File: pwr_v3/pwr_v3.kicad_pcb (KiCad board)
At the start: 4 copper layers, 166 x 166 mm, 83 parts, among them CN11 Conn_02x36_Odd_Even, CN12 Conn_02x36_Odd_Even, J1 Conn_01x12, J5 530470610, M1 Conn_02x03_Counter_Clockwise, M2 Conn_02x03_Counter_Clockwise, M3 Conn_02x03_Counter_Clockwise, M4 Conn_02x03_Counter_Clockwise, Q1 BUK9832-55A, Q2 BSS84, SW1 SW_SPST, U1 LM2576S-5, U2 LM2576S-12, U3 LM2576S-3.3, U4 LSM6DSLTR

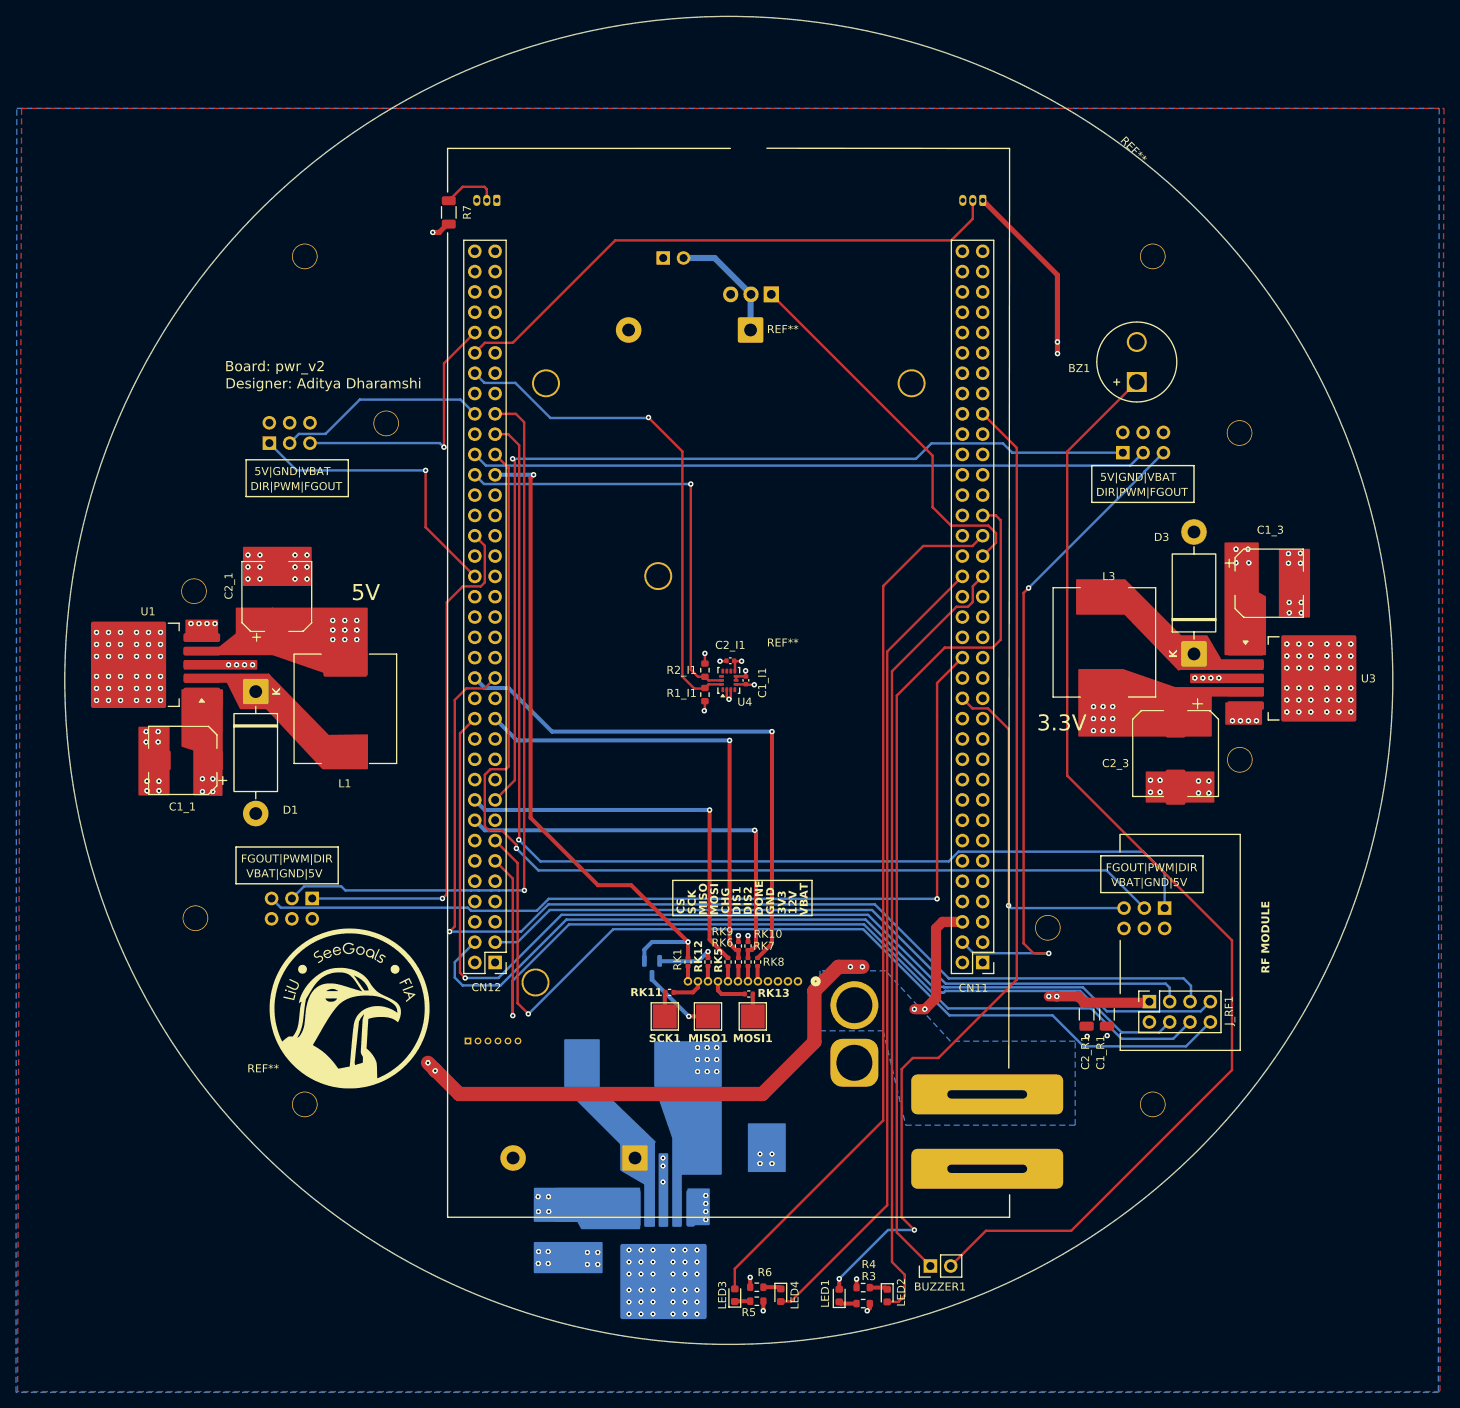
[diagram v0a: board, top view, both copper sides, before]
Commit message: Schematic and layout updated
Sch - Unwanted global labels removed from IMU, added new kicker labels, changed kicker connector footprint.
Layout - Updated kicker and encoder positions, routing updated.
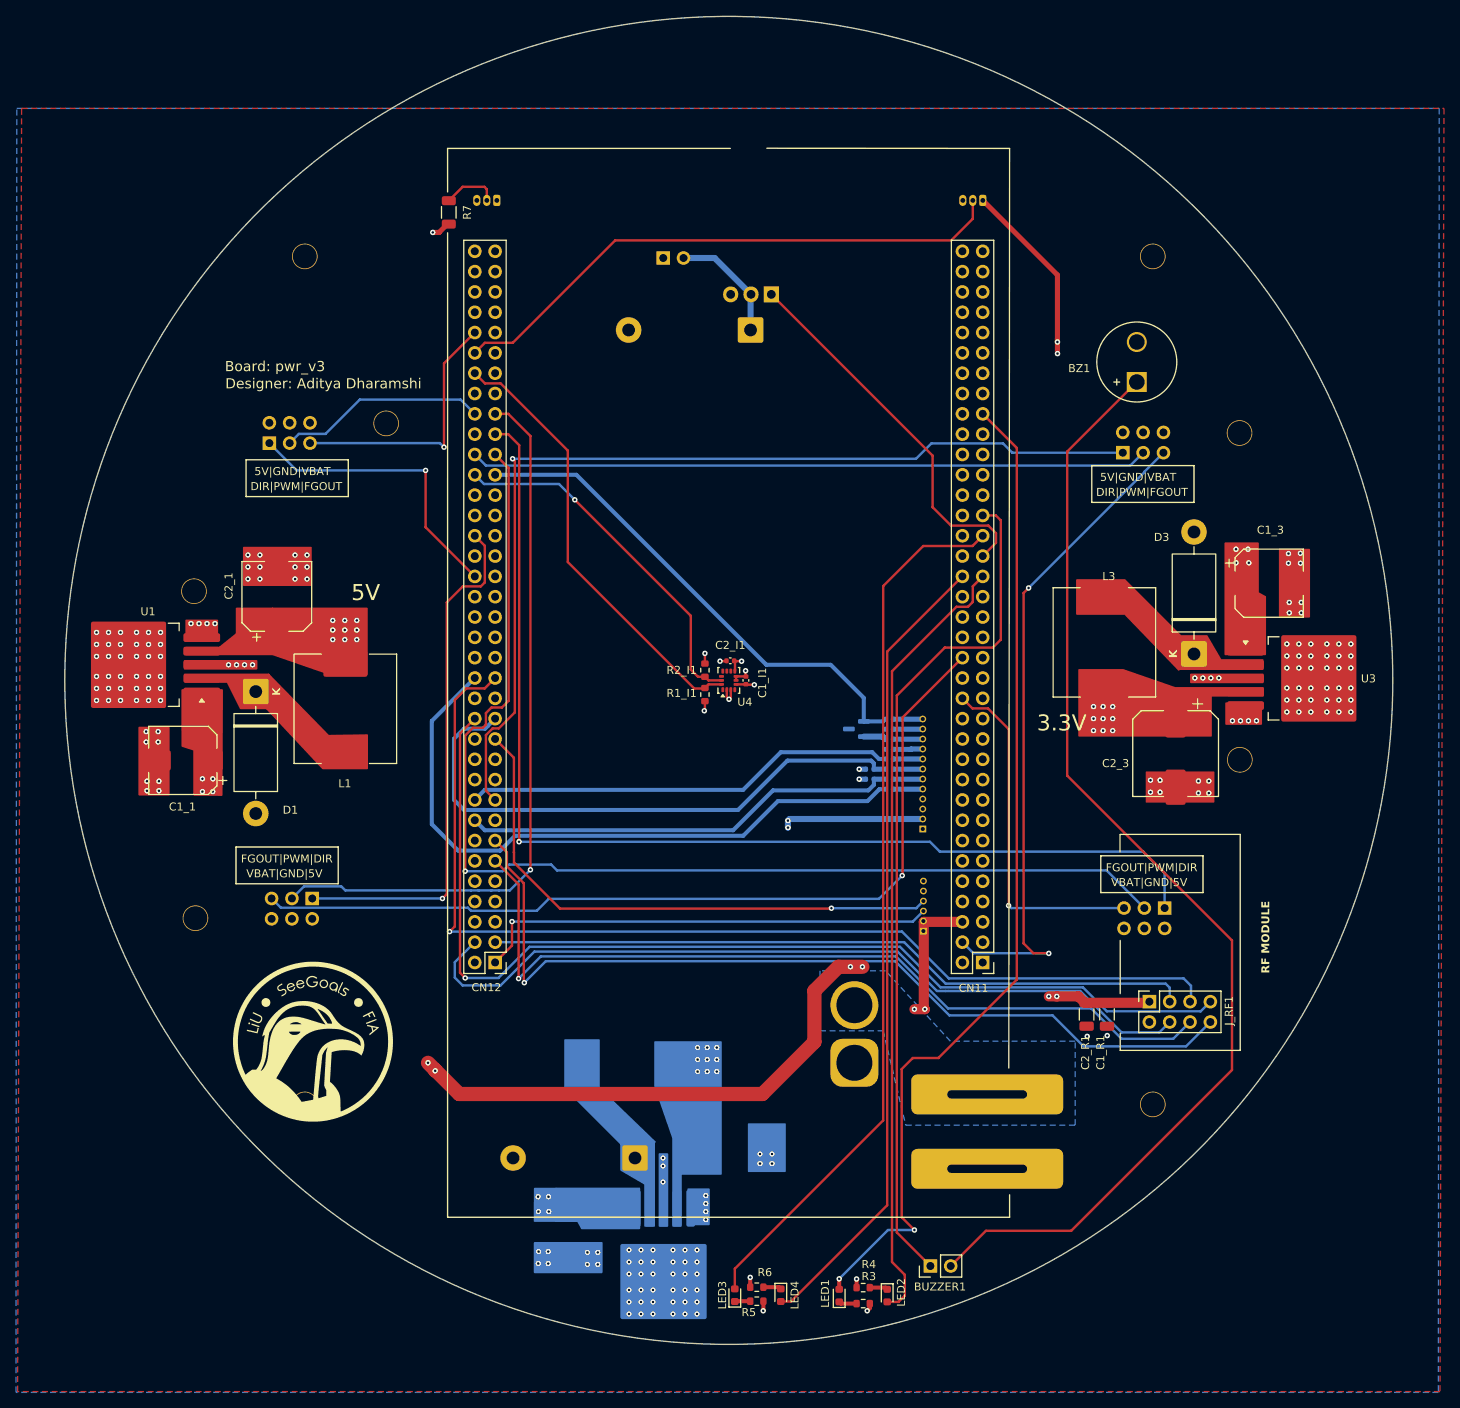
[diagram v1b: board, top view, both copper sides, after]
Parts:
- removed MH_42, NM1, NM2, NM3, NM4: , 
- removed MISO1, MOSI1, SCK1: TestPoint, TestPoint:TestPoint_Pad_3.0x3.0mm
- removed the REF** at (156.8, 86.0)
- J1: footprint CON12_1X12_UR_DF13:CON12_1X12_UR_DF13 -> 530471210_12p:530471210
- RK1, RK10, RK11, RK12, RK13, RK5, RK6, RK7, RK8, RK9: moved to B.Cu
- moved J5 58.6 mm to (174.3, 131.3), turned to -90 degrees
- moved RK11 42.8 mm to (170.1, 106.1)
- moved RK1 39.4 mm to (170.1, 104.8), turned to 180 degrees
- moved Q2 39.3 mm to (165.9, 106.1), turned to 180 degrees
- moved RK12 35.9 mm to (170.1, 107.3), turned to 180 degrees
- moved RK13 35.3 mm to (170.1, 108.6), turned to 180 degrees
- moved RK5 32.4 mm to (170.1, 109.8), turned to 180 degrees
- moved RK6 30.6 mm to (170.1, 111.1), turned to 180 degrees
- moved RK7 28.9 mm to (170.1, 112.3), turned to 180 degrees
- moved RK9 27.5 mm to (167.6, 111.1), turned to 0 degrees
- moved RK8 27.2 mm to (170.1, 113.6), turned to 180 degrees
- moved RK10 25.8 mm to (167.6, 112.3), turned to 0 degrees
- moved J1 24.6 mm to (174.2, 118.6), turned to -90 degrees
- moved G*** 7.45 mm to (148.9, 83.5)
- moved G*** 6.18 mm to (98.0, 145.2)
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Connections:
- Q2 pad 3: Net-(Q2-D) -> /KickerBoard/MISO
- RK11 pad 2: Net-(RK11-Pad2) -> /KickerBoard/SCK
- RK13 pad 2: Net-(MOSI1-Pad1) -> /KickerBoard/MOSI
- U4 pad 1: /IMU/SDO_SAO -> unconnected-(U4-SDO/SA0-Pad1)
- U4 pad 12: /IMU/CS -> unconnected-(U4-CS-Pad12)
- U4 pad 4: /IMU/INT1 -> unconnected-(U4-INT1-Pad4)
- U4 pad 9: /IMU/INT2 -> unconnected-(U4-INT2-Pad9)
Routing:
- net /STM32/ENC_SCL: track 0.00 -> 70.4 mm, vias 0 -> 1
- net 3V3: track 178.5 -> 115.2 mm
- net /STM32/ENC_SDA: track 0.00 -> 58.0 mm, vias 0 -> 1
- net 12V: track 16.5 -> 54.4 mm, vias 9 -> 11
- net /KickerBoard/CS: track 83.3 -> 63.4 mm, vias 2 -> 0
- net /KickerBoard/DIS1: track 58.3 -> 71.7 mm, vias 1 -> 0
- net /RF/SCK: track 119.0 -> 106.1 mm
- net /KickerBoard/DONE: track 69.0 -> 81.7 mm, vias 1 -> 0
- net /IMU/SCL: track 55.1 -> 45.4 mm
- net Net-(Q2-D): track 9.38 -> 0.00 mm, vias 1 -> 0
- net /RF/MISO: track 120.4 -> 111.8 mm
- net /IMU/SDA: track 64.0 -> 55.5 mm, vias 1 -> 0
- net /STM32/MOTOR4_PWM: track 136.5 -> 144.0 mm
- net /KickerBoard/CHG: track 49.3 -> 54.1 mm, vias 1 -> 0
- net Net-(Q2-S): track 7.35 -> 2.79 mm, vias 1 -> 0
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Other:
- board text added: "Board: pwr_v3"
- board text added: "ENC"
- board text removed: "Board: pwr_v2"

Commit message: Finalized files
Final files used for fabrication. Docs and Images added for easy view.
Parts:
- removed the REF** at (194.0, 40.3)
- removed the REF** at (91.8, 139.2)
- added IR_1: Conn_01x02, Connector_PinHeader_2.54mm:PinHeader_1x02_P2.54mm_Vertical, F.Cu at (105.8, 43.0)
- added MH_42: , , F.Cu at (189.9, 130.9)
- REF**: value MountingHole_8.4mm_M8 -> Custom
- moved G*** 6.31 mm to (93.1, 141.2)
- moved R7 5.15 mm to (110.0, 42.8), turned to 0 degrees
- moved REF** 3.46 mm to (150.6, 65.0)
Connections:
- CN11 pad 11: unconnected-(CN11-Pin_11-Pad11) -> /KickerBoard/SCK
- CN11 pad 54: unconnected-(CN11-Pin_54-Pad54) -> /KickerBoard/MISO
- CN11 pad 56: unconnected-(CN11-Pin_56-Pad56) -> /KickerBoard/MOSI
- IR1 pad 1: 3V3 -> GND
- IR1 pad 3: GND -> 3V3
- IR2 pad 1: GND -> unconnected-(IR2-Pin_1-Pad1)
- IR2 pad 3: unconnected-(IR2-Pin_3-Pad3) -> GND
- J5 pad 1: 5V -> GND
- J5 pad 2: 5V -> GND
- J5 pad 3: /STM32/ENC_SDA -> /STM32/ENC_SCL
- J5 pad 4: /STM32/ENC_SCL -> /STM32/ENC_SDA
- J5 pad 5: GND -> 5V
- J5 pad 6: GND -> 5V
- R7 pad 1: 5V -> Net-(IR_1-Pin_1)
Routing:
- net /KickerBoard/MOSI: track 0.00 -> 54.5 mm, vias 0 -> 1
- net 3V3: track 115.2 -> 159.8 mm
- net /KickerBoard/MISO: track 0.00 -> 44.0 mm, vias 0 -> 1
- net /KickerBoard/SCK: track 0.00 -> 33.0 mm, vias 0 -> 2
- net Net-(BUZZER1-Pin_2): track 143.5 -> 130.6 mm
- net /STM32/IR_detect: track 71.7 -> 84.3 mm
- net 5V: track 419.9 -> 427.1 mm, vias 16 -> 15
- net /STM32/MOTOR1_FGOUT: track 83.6 -> 76.6 mm
- net /STM32/MOTOR2_FGOUT: track 32.9 -> 26.3 mm, vias 1 -> 0
- net /RF/MISO: track 111.8 -> 106.3 mm
- net /STM32/BUZZER: track 106.4 -> 101.3 mm
- net /STM32/MOTOR4_PWM: track 144.0 -> 148.4 mm
- net Net-(IR2-Pin_2): track 6.99 -> 11.4 mm
- net /STM32/DRIBBLER_CONTROL: track 47.8 -> 52.2 mm, vias 0 -> 1
- net /STM32/MOTOR2_DIR: track 36.7 -> 32.6 mm, vias 1 -> 0
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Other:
- board text added: "5V 5V SDA SCL GND GND"
- board text added: "Board: pwr_v3 (2026)"
- board text added: "GND|DET|3V3"
- board text added: "GND|VBAT"
- board text added: "x|5V|GND"
- board text removed: "-|GND|IN"
- board text removed: "Board: pwr_v3"
- board text removed: "GND|OUT|3V3"
- board text removed: "TX|VBAT"
